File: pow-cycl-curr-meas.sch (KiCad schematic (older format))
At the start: 46 parts, among them Q1 SQS401EN-T1_BE3, Q10 SSM3K15ACT, Q2 SQS401EN-T1_BE3, Q3 SSM3K15ACT, Q4 SSM3K15ACT, Q5 SQS401EN-T1_BE3, Q6 SSM3K15ACT, Q7 SQS401EN-T1_BE3, Q8 SQS401EN-T1_BE3, Q9 SSM3K15ACT, U10 TCA9534, U11 TMCS1100A2-Q1, U12 TMCS1100A2-Q1, U13 TMCS1100A2-Q1, U14 ADS7828, U8 TMCS1100A2-Q1, U9 TMCS1100A2-Q1

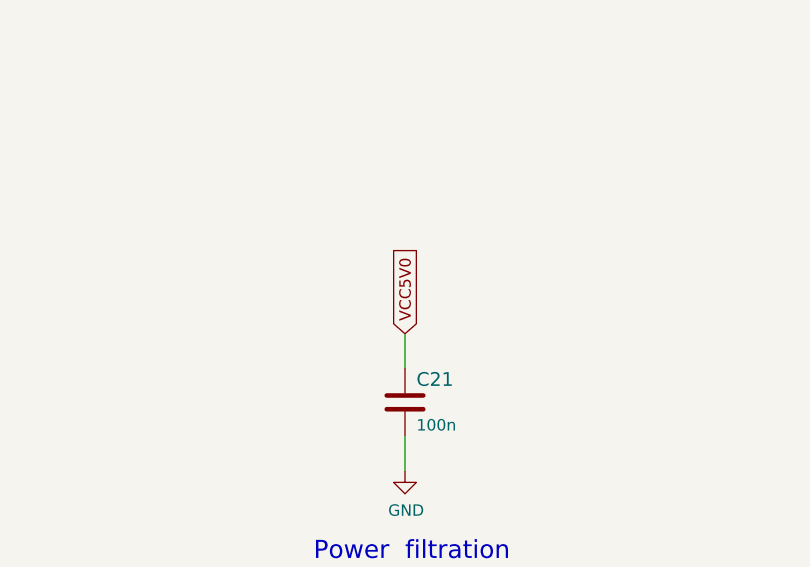
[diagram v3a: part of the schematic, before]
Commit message: Initial routing. Small schematics improvements
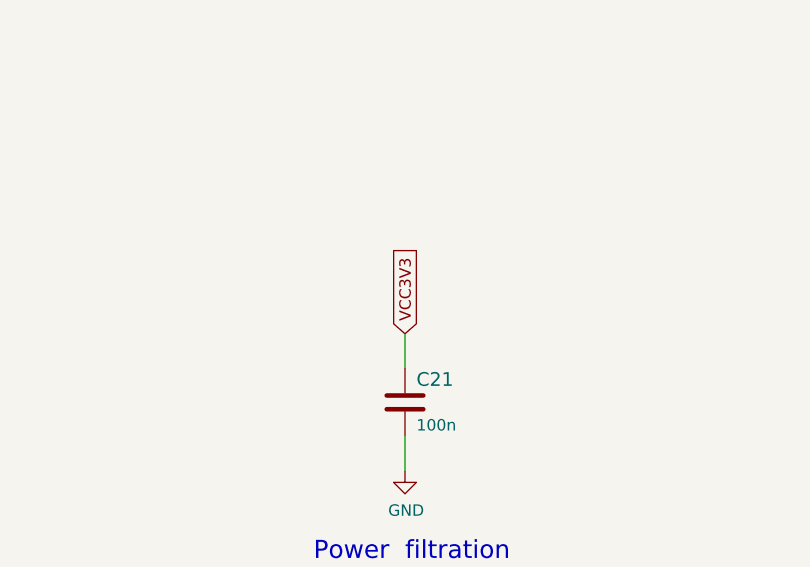
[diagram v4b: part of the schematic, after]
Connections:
- net VCC5V0 is gone; now on net VCC3V3: C21.1
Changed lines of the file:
@@
 $EndComp
 Text GLabel 13300 6900 1    50   Input ~ 0
-VCC5V0
+VCC3V3
 $Comp
 L power:GND #PWR058
